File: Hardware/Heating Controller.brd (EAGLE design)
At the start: 160 x 100 mm, 28 parts, among them IC1 ATMega 328p-pu, IC2 ULN2003AD, K1 G5LE, K2 G5LE, Q1 16MHz, X1 SWITCHED_OUT, X2 MAINS IN, X3 NEUTRAL

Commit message: added optocoupled output to add extra layer of isolation
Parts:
- added OK1, OK2: LTV816S, optocoupler:SMD4
- added R5, R6, R7, R8: (no value), rcl:R1206W
- C2: device rcl:C025-025X050 -> rcl:C1206K
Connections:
- new net AGND: IC2.5, IC2.6, IC2.7, IC2.8
- new net N$11: OK1.1, R5.1
- new net N$14: OK2.1, R6.1
- new net N$20: OK1.4, R7.2
- new net N$21: OK2.4, R8.2
- new net N$22: IC2.1, IC2.2, OK1.3
- new net N$23: IC2.3, IC2.4, OK2.3
- new net VCC: IC2.9, K1.1, K2.1, R7.1, R8.1
- net +3V3: no longer IC2.9, K1.1, K2.1
- net GND: now also OK1.2, OK2.2; no longer IC2.5, IC2.6, IC2.7, IC2.8
- net HEATING_R: now also R6.2; no longer IC2.3, IC2.4
- net HOTWATER_R: now also R5.2; no longer IC2.1, IC2.2

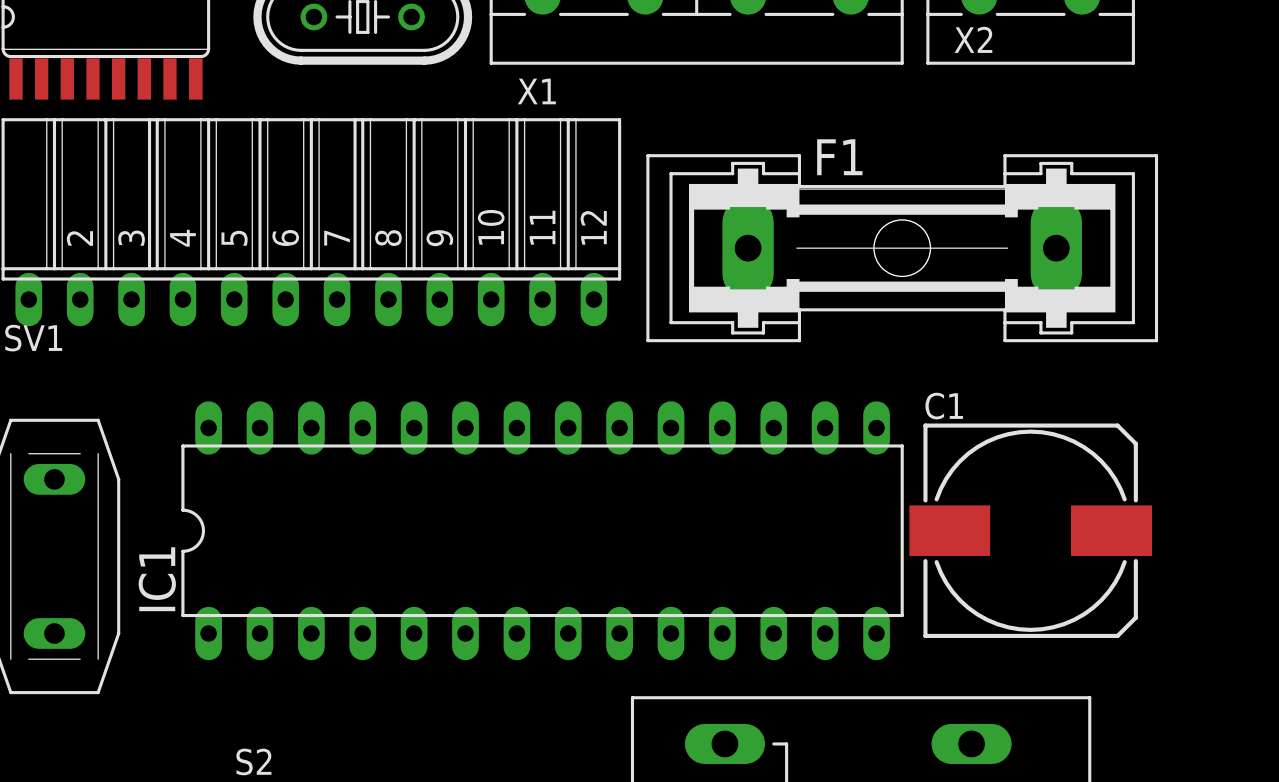
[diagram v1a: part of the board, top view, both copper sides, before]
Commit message: Updated wrong fuse holder and processor footprint
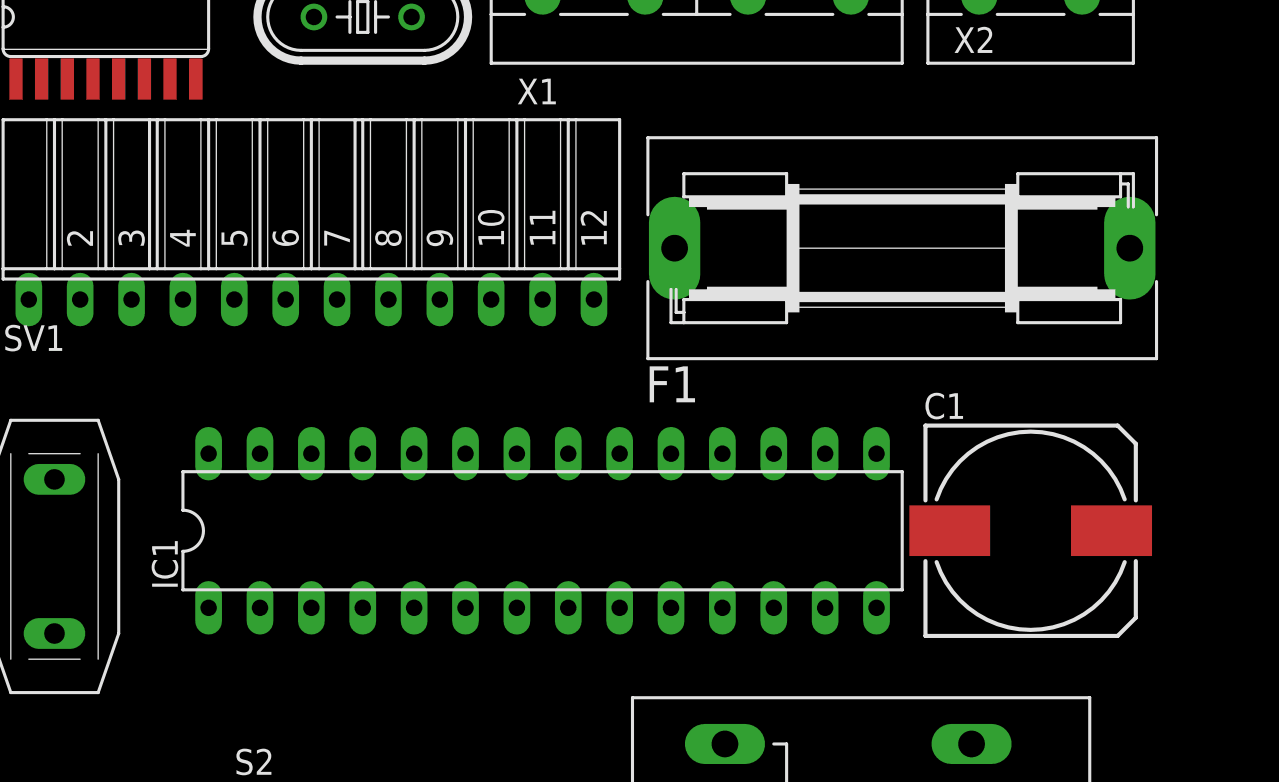
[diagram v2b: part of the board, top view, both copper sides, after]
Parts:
- F1: device fuse:GSH15 -> fuse:SH22,5A
- IC1: device ic-package:DIL28-4 -> ic-package:DIL28-3
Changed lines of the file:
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@@
 <elements>
 <element name="U$1" library="VTX214001103" package="VTX214001103" value="VTX-214-001-103" x="-25.4" y="12.7"/>
-<element name="F1" library="fuse" package="GSH15" value="230V 70mA" x="-25.4" y="64.77">
-<attribute name="OC_NEWARK" value="02P0318" x="0" y="0" size="1.778" layer="27" display="off"/>
-<attribute name="MPN" value="64900001039" x="0" y="0" size="1.778" layer="27" display="off"/>
-<attribute name="MF" value="" x="0" y="0" size="1.778" layer="27" display="off"/>
-<attribute name="OC_FARNELL" value="1271673" x="0" y="0" size="1.778" layer="27" display="off"/>
+<element name="F1" library="fuse" package="SH22,5A" value="230V 70mA" x="-25.4" y="64.77">
+<attribute name="OC_NEWARK" value="04F1224" x="0" y="0" size="1.778" layer="27" display="off"/>
+<attribute name="MPN" value="0031.7701.11" x="0" y="0" size="1.778" layer="27" display="off"/>
+<attribute name="MF" value="" x="0" y="0" size="1.778" layer="27" display="off"/>
+<attribute name="OC_FARNELL" value="unknown" x="0" y="0" size="1.778" layer="27" display="off"/>
 </element>
 <element name="R1" library="varistor" package="P594" value="P594" x="-67.31" y="49.53"/>
@@
 <element name="LED1" library="led" package="LED5MM" value="HEAT" x="-58.42" y="87.63"/>
 <element name="LED2" library="led" package="LED5MM" value="WATER" x="-45.72" y="87.63"/>
-<element name="IC1" library="ic-package" package="DIL28-4" value="ATMega 328p-pu" x="-43.18" y="50.8"/>
+<element name="IC1" library="ic-package" package="DIL28-3" value="ATMega 328p-pu" x="-43.18" y="50.8"/>
 <element name="Q1" library="crystal" package="HC49/S" value="16MHz" x="-52.07" y="76.2">
 <attribute name="OC_NEWARK" value="unknown" x="0" y="0" size="1.778" layer="27" display="off"/>
@@
 <contactref element="F1" pad="1"/>
 <contactref element="X2" pad="1"/>
-<wire x1="-33.02" y1="64.77" x2="-21.59" y2="78.105" width="0" layer="19" extent="1-1"/>
+<wire x1="-36.6522" y1="64.77" x2="-21.59" y2="78.105" width="0" layer="19" extent="1-1"/>
 </signal>
 <signal name="N$2">
@@
 <contactref element="C2" pad="1"/>
 <contactref element="R1" pad="2"/>
-<wire x1="-67.31" y1="45.72" x2="-17.78" y2="64.77" width="0" layer="19" extent="1-1"/>
+<wire x1="-67.31" y1="45.72" x2="-14.1478" y2="64.77" width="0" layer="19" extent="1-1"/>
 <wire x1="-70.08" y1="87.63" x2="-67.31" y2="45.72" width="0" layer="19" extent="1-1"/>
 <wire x1="-34.15" y1="3.2" x2="-67.31" y2="45.72" width="0" layer="19" extent="1-1"/>
@@
 <wire x1="-31.98" y1="93.98" x2="-13.741" y2="95.25" width="0" layer="19" extent="1-1"/>
 <wire x1="-40.64" y1="62.23" x2="-31.98" y2="93.98" width="0" layer="19" extent="1-1"/>
-<wire x1="-39.37" y1="55.88" x2="-40.64" y2="62.23" width="0" layer="19" extent="1-1"/>
-<wire x1="-41.91" y1="55.88" x2="-39.37" y2="55.88" width="0" layer="19" extent="1-1"/>
-<wire x1="-44.45" y1="45.72" x2="-41.91" y2="55.88" width="0" layer="19" extent="1-1"/>
-<wire x1="-15.05" y1="50.8" x2="-39.37" y2="55.88" width="0" layer="19" extent="1-1"/>
+<wire x1="-39.37" y1="54.61" x2="-40.64" y2="62.23" width="0" layer="19" extent="1-1"/>
+<wire x1="-41.91" y1="54.61" x2="-39.37" y2="54.61" width="0" layer="19" extent="1-1"/>
+<wire x1="-44.45" y1="46.99" x2="-41.91" y2="54.61" width="0" layer="19" extent="1-1"/>
+<wire x1="-15.05" y1="50.8" x2="-39.37" y2="54.61" width="0" layer="19" extent="1-1"/>
 <wire x1="-16.65" y1="22.2" x2="-15.05" y2="50.8" width="0" layer="19" extent="1-1"/>
 </signal>
@@
 <wire x1="-59.5884" y1="34.2392" x2="-67.4116" y2="34.2392" width="0" layer="19" extent="1-1"/>
 <wire x1="-47.0916" y1="34.2392" x2="-59.5884" y2="34.2392" width="0" layer="19" extent="1-1"/>
-<wire x1="-41.91" y1="45.72" x2="-47.0916" y2="34.2392" width="0" layer="19" extent="1-1"/>
-<wire x1="-44.45" y1="55.88" x2="-41.91" y2="45.72" width="0" layer="19" extent="1-1"/>
-<wire x1="-60.96" y1="62.23" x2="-44.45" y2="55.88" width="0" layer="19" extent="1-1"/>
-<wire x1="-23.05" y1="50.8" x2="-41.91" y2="45.72" width="0" layer="19" extent="1-1"/>
+<wire x1="-41.91" y1="46.99" x2="-47.0916" y2="34.2392" width="0" layer="19" extent="1-1"/>
+<wire x1="-44.45" y1="54.61" x2="-41.91" y2="46.99" width="0" layer="19" extent="1-1"/>
+<wire x1="-60.96" y1="62.23" x2="-44.45" y2="54.61" width="0" layer="19" extent="1-1"/>
+<wire x1="-23.05" y1="50.8" x2="-41.91" y2="46.99" width="0" layer="19" extent="1-1"/>
 <wire x1="-57.15" y1="87.63" x2="-60.96" y2="62.23" width="0" layer="19" extent="1-1"/>
 <wire x1="-44.45" y1="87.63" x2="-57.15" y2="87.63" width="0" layer="19" extent="1-1"/>
@@
 <contactref element="IC1" pad="1"/>
 <contactref element="R2" pad="1"/>
-<wire x1="-59.69" y1="45.72" x2="-16.739" y2="95.25" width="0" layer="19" extent="1-1"/>
+<wire x1="-59.69" y1="46.99" x2="-16.739" y2="95.25" width="0" layer="19" extent="1-1"/>
 </signal>
 <signal name="RXD">
 <contactref element="IC1" pad="2"/>
 <contactref element="SV1" pad="2"/>
-<wire x1="-66.04" y1="62.23" x2="-57.15" y2="45.72" width="0" layer="19" extent="1-1"/>
+<wire x1="-66.04" y1="62.23" x2="-57.15" y2="46.99" width="0" layer="19" extent="1-1"/>
 </signal>
 <signal name="TXD">
 <contactref element="IC1" pad="3"/>
 <contactref element="SV1" pad="3"/>
-<wire x1="-63.5" y1="62.23" x2="-54.61" y2="45.72" width="0" layer="19" extent="1-1"/>
+<wire x1="-63.5" y1="62.23" x2="-54.61" y2="46.99" width="0" layer="19" extent="1-1"/>
 </signal>
 <signal name="N$5">
@@
 <contactref element="C3" pad="1"/>
 <wire x1="-49.657" y1="76.2" x2="-21.82" y2="93.98" width="0" layer="19" extent="1-1"/>
-<wire x1="-39.37" y1="45.72" x2="-49.657" y2="76.2" width="0" layer="19" extent="1-1"/>
+<wire x1="-39.37" y1="46.99" x2="-49.657" y2="76.2" width="0" layer="19" extent="1-1"/>
 </signal>
 <signal name="N$6">
@@
 <contactref element="IC1" pad="10"/>
 <wire x1="-54.483" y1="76.2" x2="-26.9" y2="93.98" width="0" layer="19" extent="1-1"/>
-<wire x1="-36.83" y1="45.72" x2="-54.483" y2="76.2" width="0" layer="19" extent="1-1"/>
+<wire x1="-36.83" y1="46.99" x2="-54.483" y2="76.2" width="0" layer="19" extent="1-1"/>
 </signal>
 <signal name="CSN2">
 <contactref element="IC1" pad="14"/>
 <contactref element="SV1" pad="11"/>
-<wire x1="-43.18" y1="62.23" x2="-26.67" y2="45.72" width="0" layer="19" extent="1-1"/>
+<wire x1="-43.18" y1="62.23" x2="-26.67" y2="46.99" width="0" layer="19" extent="1-1"/>
 </signal>
 <signal name="INT">
 <contactref element="IC1" pad="13"/>
 <contactref element="SV1" pad="8"/>
-<wire x1="-50.8" y1="62.23" x2="-29.21" y2="45.72" width="0" layer="19" extent="1-1"/>
+<wire x1="-50.8" y1="62.23" x2="-29.21" y2="46.99" width="0" layer="19" extent="1-1"/>
 </signal>
 <signal name="SCK">
 <contactref element="IC1" pad="19"/>
 <contactref element="SV1" pad="9"/>
-<wire x1="-48.26" y1="62.23" x2="-36.83" y2="55.88" width="0" layer="19" extent="1-1"/>
+<wire x1="-48.26" y1="62.23" x2="-36.83" y2="54.61" width="0" layer="19" extent="1-1"/>
 </signal>
 <signal name="MISO">
 <contactref element="IC1" pad="18"/>
 <contactref element="SV1" pad="10"/>
-<wire x1="-45.72" y1="62.23" x2="-34.29" y2="55.88" width="0" layer="19" extent="1-1"/>
+<wire x1="-45.72" y1="62.23" x2="-34.29" y2="54.61" width="0" layer="19" extent="1-1"/>
 </signal>
 <signal name="MOSI">
 <contactref element="IC1" pad="17"/>
 <contactref element="SV1" pad="7"/>
-<wire x1="-53.34" y1="62.23" x2="-31.75" y2="55.88" width="0" layer="19" extent="1-1"/>
+<wire x1="-53.34" y1="62.23" x2="-31.75" y2="54.61" width="0" layer="19" extent="1-1"/>
 </signal>
 <signal name="CE">
 <contactref element="IC1" pad="16"/>
 <contactref element="SV1" pad="5"/>
-<wire x1="-58.42" y1="62.23" x2="-29.21" y2="55.88" width="0" layer="19" extent="1-1"/>
+<wire x1="-58.42" y1="62.23" x2="-29.21" y2="54.61" width="0" layer="19" extent="1-1"/>
 </signal>
 <signal name="CSN">
 <contactref element="IC1" pad="15"/>
 <contactref element="SV1" pad="6"/>
-<wire x1="-55.88" y1="62.23" x2="-26.67" y2="55.88" width="0" layer="19" extent="1-1"/>
+<wire x1="-55.88" y1="62.23" x2="-26.67" y2="54.61" width="0" layer="19" extent="1-1"/>
 </signal>
 <signal name="HEATL">
 <contactref element="IC1" pad="11"/>
 <contactref element="R4" pad="2"/>
-<wire x1="-79.781" y1="86.36" x2="-34.29" y2="45.72" width="0" layer="19" extent="1-1"/>
+<wire x1="-79.781" y1="86.36" x2="-34.29" y2="46.99" width="0" layer="19" extent="1-1"/>
 </signal>
 <signal name="HOTWATERL">
 <contactref element="IC1" pad="12"/>
 <contactref element="R3" pad="2"/>
-<wire x1="-73.431" y1="86.36" x2="-31.75" y2="45.72" width="0" layer="19" extent="1-1"/>
+<wire x1="-73.431" y1="86.36" x2="-31.75" y2="46.99" width="0" layer="19" extent="1-1"/>
 </signal>
 <signal name="N$7">
@@
 <contactref element="IC1" pad="4"/>
 <contactref element="R5" pad="2"/>
-<wire x1="-52.07" y1="45.72" x2="-97.561" y2="-3.81" width="0" layer="19" extent="1-1"/>
+<wire x1="-52.07" y1="46.99" x2="-97.561" y2="-3.81" width="0" layer="19" extent="1-1"/>
 </signal>
 <signal name="HEATING_R">
 <contactref element="IC1" pad="5"/>
 <contactref element="R6" pad="2"/>
-<wire x1="-49.53" y1="45.72" x2="-97.561" y2="-10.16" width="0" layer="19" extent="1-1"/>
+<wire x1="-49.53" y1="46.99" x2="-97.561" y2="-10.16" width="0" layer="19" extent="1-1"/>
 </signal>
 <signal name="N$9">
@@
 <contactref element="S1" pad="4"/>
 <wire x1="-67.4116" y1="29.2608" x2="-79.9084" y2="29.2608" width="0" layer="19" extent="1-1"/>
-<wire x1="-59.69" y1="55.88" x2="-67.4116" y2="29.2608" width="0" layer="19" extent="1-1"/>
+<wire x1="-59.69" y1="54.61" x2="-67.4116" y2="29.2608" width="0" layer="19" extent="1-1"/>
 </signal>
 <signal name="N$10">
@@
 <contactref element="S2" pad="4"/>
 <wire x1="-47.0916" y1="29.2608" x2="-59.5884" y2="29.2608" width="0" layer="19" extent="1-1"/>
-<wire x1="-57.15" y1="55.88" x2="-59.5884" y2="29.2608" width="0" layer="19" extent="1-1"/>
+<wire x1="-57.15" y1="54.61" x2="-59.5884" y2="29.2608" width="0" layer="19" extent="1-1"/>
 </signal>
 <signal name="N$12">

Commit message: Inital Mockup of board component placement
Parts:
- added L1, L2: (no value), rcl:L1812
- C1: value 10u -> 47u; device rcl:153CLV-1010 -> resistor:E2,5-7
- C2: device rcl:C1206K -> capacitor-wima:C15B5
- moved X3 176.8 mm to (90.2, 6.35)
- moved R8 164.4 mm to (52.1, 41.9), flipped to the bottom, turned to 90 degrees
- moved R6 161.4 mm to (48.3, 55.9), flipped to the bottom
- moved OK2 157.5 mm to (53.3, 49.5), flipped to the bottom, turned to 180 degrees
- moved R7 153.8 mm to (43.2, 41.9), flipped to the bottom, turned to 90 degrees
- moved R5 148.6 mm to (38.1, 53.3), flipped to the bottom
- moved IC2 142.0 mm to (73.7, 44.5), flipped to the bottom, turned to 180 degrees
- moved R4 140.7 mm to (57.1, 61.0), flipped to the bottom
- moved OK1 140.6 mm to (44.5, 49.5), flipped to the bottom, turned to 180 degrees
- moved K1 135.5 mm to (83.8, 24.1), turned to 270 degrees
- moved R3 134.0 mm to (57.1, 63.5), flipped to the bottom
- moved X1 128.9 mm to (71.1, 6.35)
- moved LED1 126.8 mm to (66.0, 63.5)
- moved H4 124.5 mm to (92.7, 86.4)
- moved LED2 116.2 mm to (66.0, 55.9)
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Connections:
- removed net AGND: IC2.5, IC2.6, IC2.7, IC2.8
- new net +3V3A: L1.1, U$1.2
- net +3V3: now also L1.2, L2.1; no longer U$1.2
- net GND: now also IC2.5, IC2.6, IC2.7, IC2.8
- net N$1: now also X2.2; no longer X2.1
- net N$15: now also X1.2; no longer X1.1
- net N$16: now also X1.1; no longer X1.2
- net N$17: now also X1.4; no longer X1.3
- net N$18: now also X1.3; no longer X1.4
- net N$3: now also X2.1; no longer X2.2
- net VCC: now also L2.2
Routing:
- net +3V3: track 0.00 -> 127.9 mm, vias 0 -> 4
- net VCC: track 0.00 -> 117.4 mm
- net N$2: track 0.00 -> 65.2 mm
- net N$9: track 0.00 -> 34.5 mm
- net MOSI: track 0.00 -> 30.9 mm
- net N$3: track 0.00 -> 30.6 mm
- net N$22: track 0.00 -> 30.1 mm
- net N$17: track 0.00 -> 30.0 mm
- net N$15: track 0.00 -> 29.5 mm
- net INT: track 0.00 -> 29.4 mm
- net N$13: track 0.00 -> 27.5 mm
- net N$10: track 0.00 -> 26.0 mm
- net CSN2: track 0.00 -> 23.3 mm
- net HEATING_R: track 0.00 -> 22.9 mm
- net CSN: track 0.00 -> 22.2 mm
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- added copper zone on layer 16, net GND
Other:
- board size 160 x 100 mm -> 96.5 x 91.1 mm

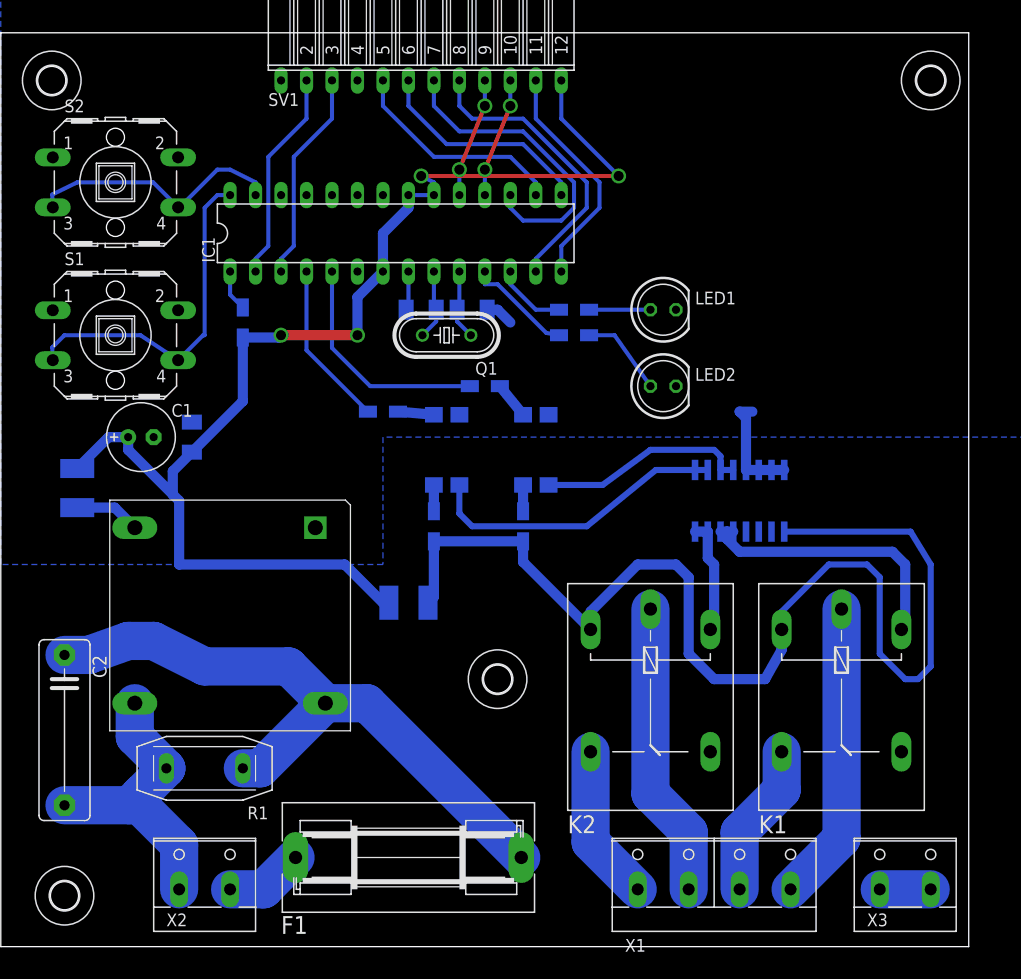
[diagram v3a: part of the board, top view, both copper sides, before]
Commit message: fixed incorrect resistor footprints. Added AGND Isolation Inductor. Added Silk Text. Moved Component Labels
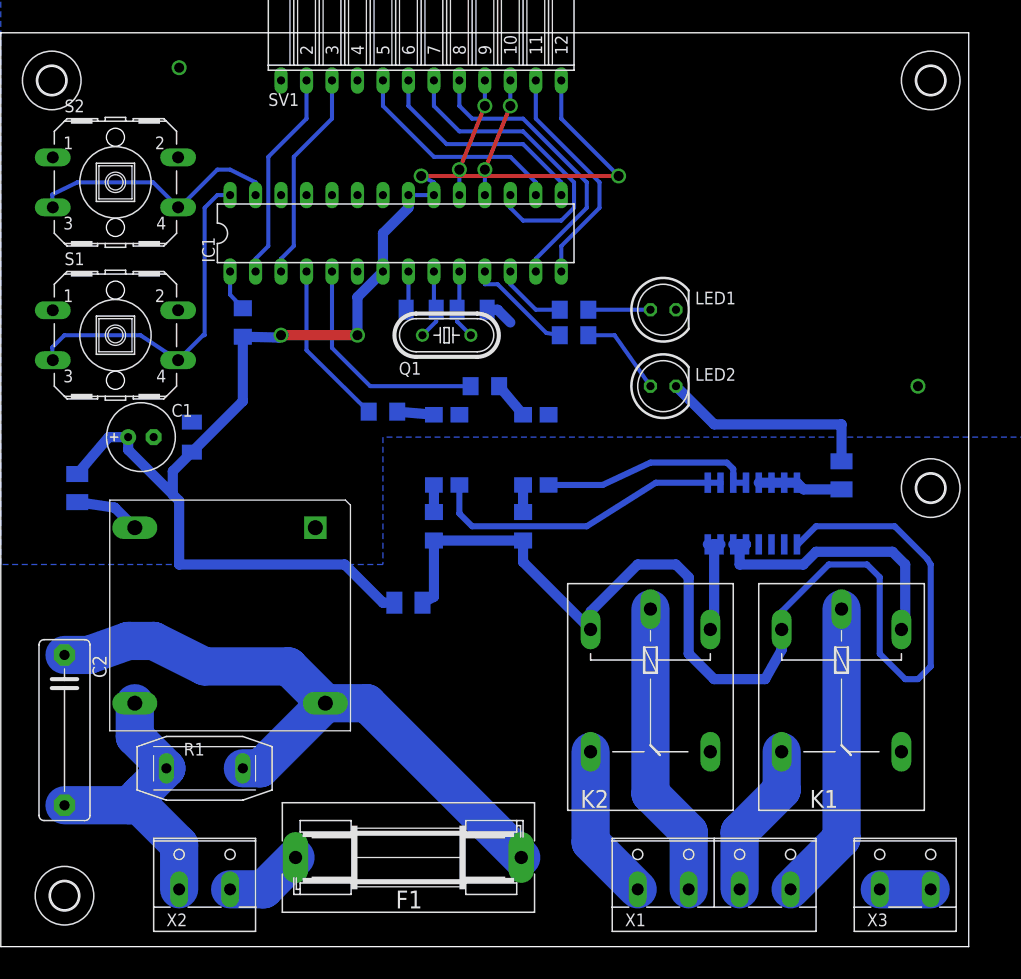
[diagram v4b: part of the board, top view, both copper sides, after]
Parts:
- added L3: (no value), rcl:L3230M
- L1, L2: device rcl:L1812 -> rcl:L3230M
- R2, R3, R4, R5, R6, R7, R8: device rcl:R1206W -> rcl:R1206
- moved H3 47.2 mm to (92.7, 45.7)
- moved IC2 1.80 mm to (74.9, 43.2)
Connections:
- new net AGND: IC2.5, IC2.6, IC2.7, IC2.8, L3.2
- net GND: now also L3.1; no longer IC2.5, IC2.6, IC2.7, IC2.8
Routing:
- net GND: track 17.9 -> 28.5 mm
- net AGND: track 0.00 -> 8.53 mm
- net N$12: track 11.4 -> 9.91 mm
- net +3V3: track 127.9 -> 128.9 mm
- net N$13: track 27.5 -> 28.1 mm
- net N$23: track 21.2 -> 21.8 mm
- net N$22: track 30.1 -> 30.7 mm
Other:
- board text added: "2015"
- board text added: "Heating Controller"
- board text added: "L"
- board text added: "MAINS"
- board text added: "N"
- board text added: "Neutral"
- board text added: "Rev A."
- board text added: "S/O1"
- board text added: "S/O2"
- board text added: "SmartHome"
